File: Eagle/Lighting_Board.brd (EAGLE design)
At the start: 21.6 x 63.5 mm, 15 parts

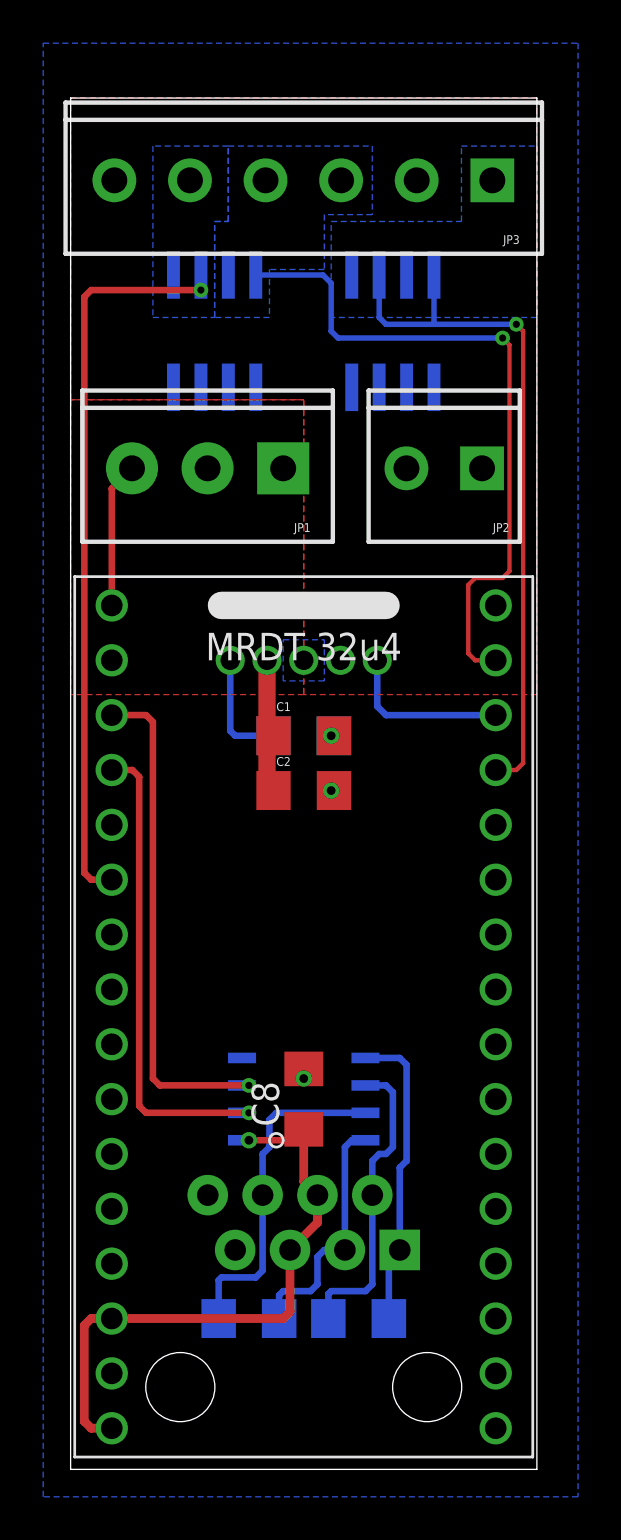
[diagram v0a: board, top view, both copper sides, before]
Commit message: Added mounting holes
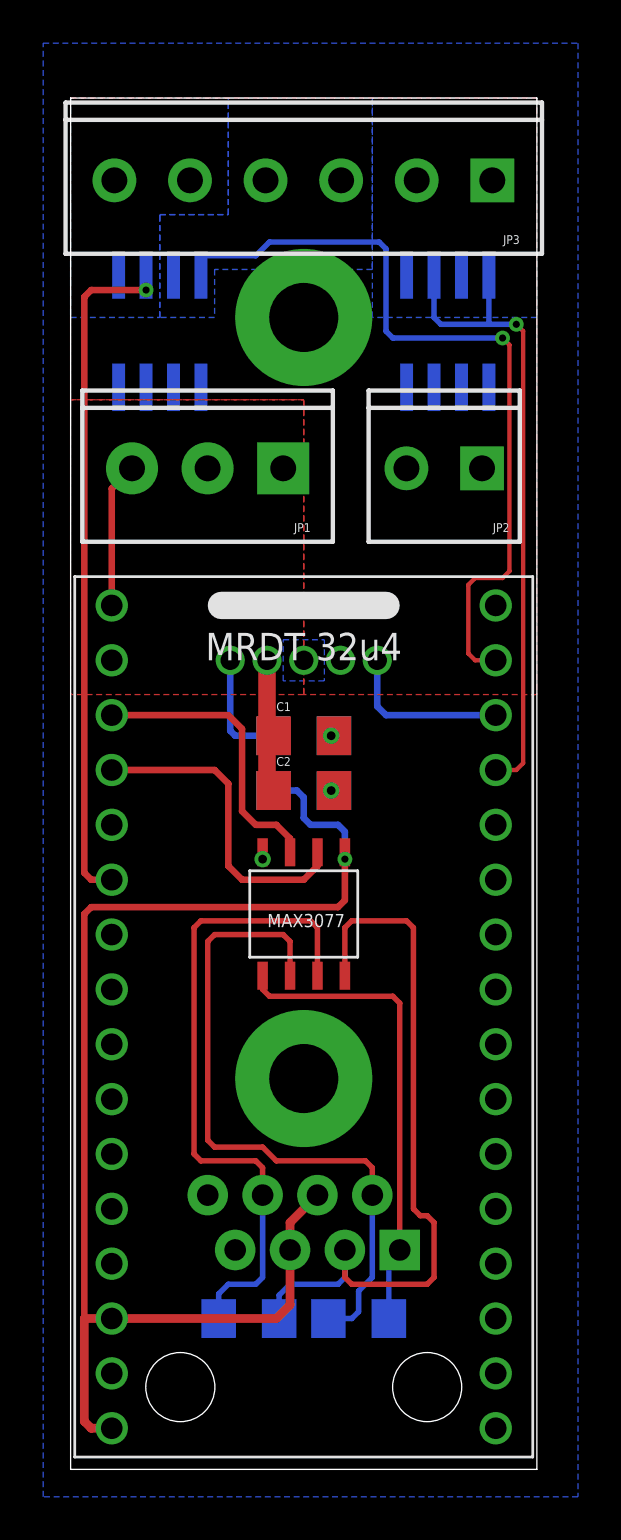
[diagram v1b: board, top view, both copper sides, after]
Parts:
- added S1, S2: STANDOFF_ELECTRICAL, SparkFun-Electromechanical:STANDOFF-ELECTRICAL
- moved C8 14.3 mm to (10.8, 31.4), flipped to the bottom, turned to 180 degrees
- moved U$3 8.57 mm to (10.8, 25.7), flipped to the top, turned to 180 degrees
- moved U$5 2.54 mm to (4.13, 52.7)
- moved U$6 2.54 mm to (17.5, 52.7)
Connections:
- net GND: now also S1.P1, S2.P1
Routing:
- net +5V: track 27.9 -> 60.8 mm
- net N$20: track 11.6 -> 33.8 mm
- net N$18: track 14.2 -> 31.5 mm
- net N$19: track 15.7 -> 30.7 mm
- net N$21: track 23.4 -> 13.5 mm, vias 1 -> 0
- net N$12: track 14.1 -> 22.1 mm
- net RXD: track 22.2 -> 14.8 mm, vias 1 -> 0
- net G2: track 31.6 -> 36.9 mm
- net G1: track 34.3 -> 31.8 mm
- net G3: track 32.6 -> 30.0 mm
